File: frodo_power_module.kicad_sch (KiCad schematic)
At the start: 84 parts, among them J1 Keystone 1048, J10 SWD Header, J2 Molex MicroFit 2x3, J3 Molex MicroFit 2x2, J4 Molex MicroFit 2x2, J5 JST-GH, J6 JST-GH, J7 Molex MicroFit 2x3, U1 STM32F042F6Px, U2 L7805, U3 AZ1117I-3.3, U4 BQ25171-Q1, U5 BQ29200, U6 MCP2562-E-SN, U7 INA213, Y1 8MHz, 12p

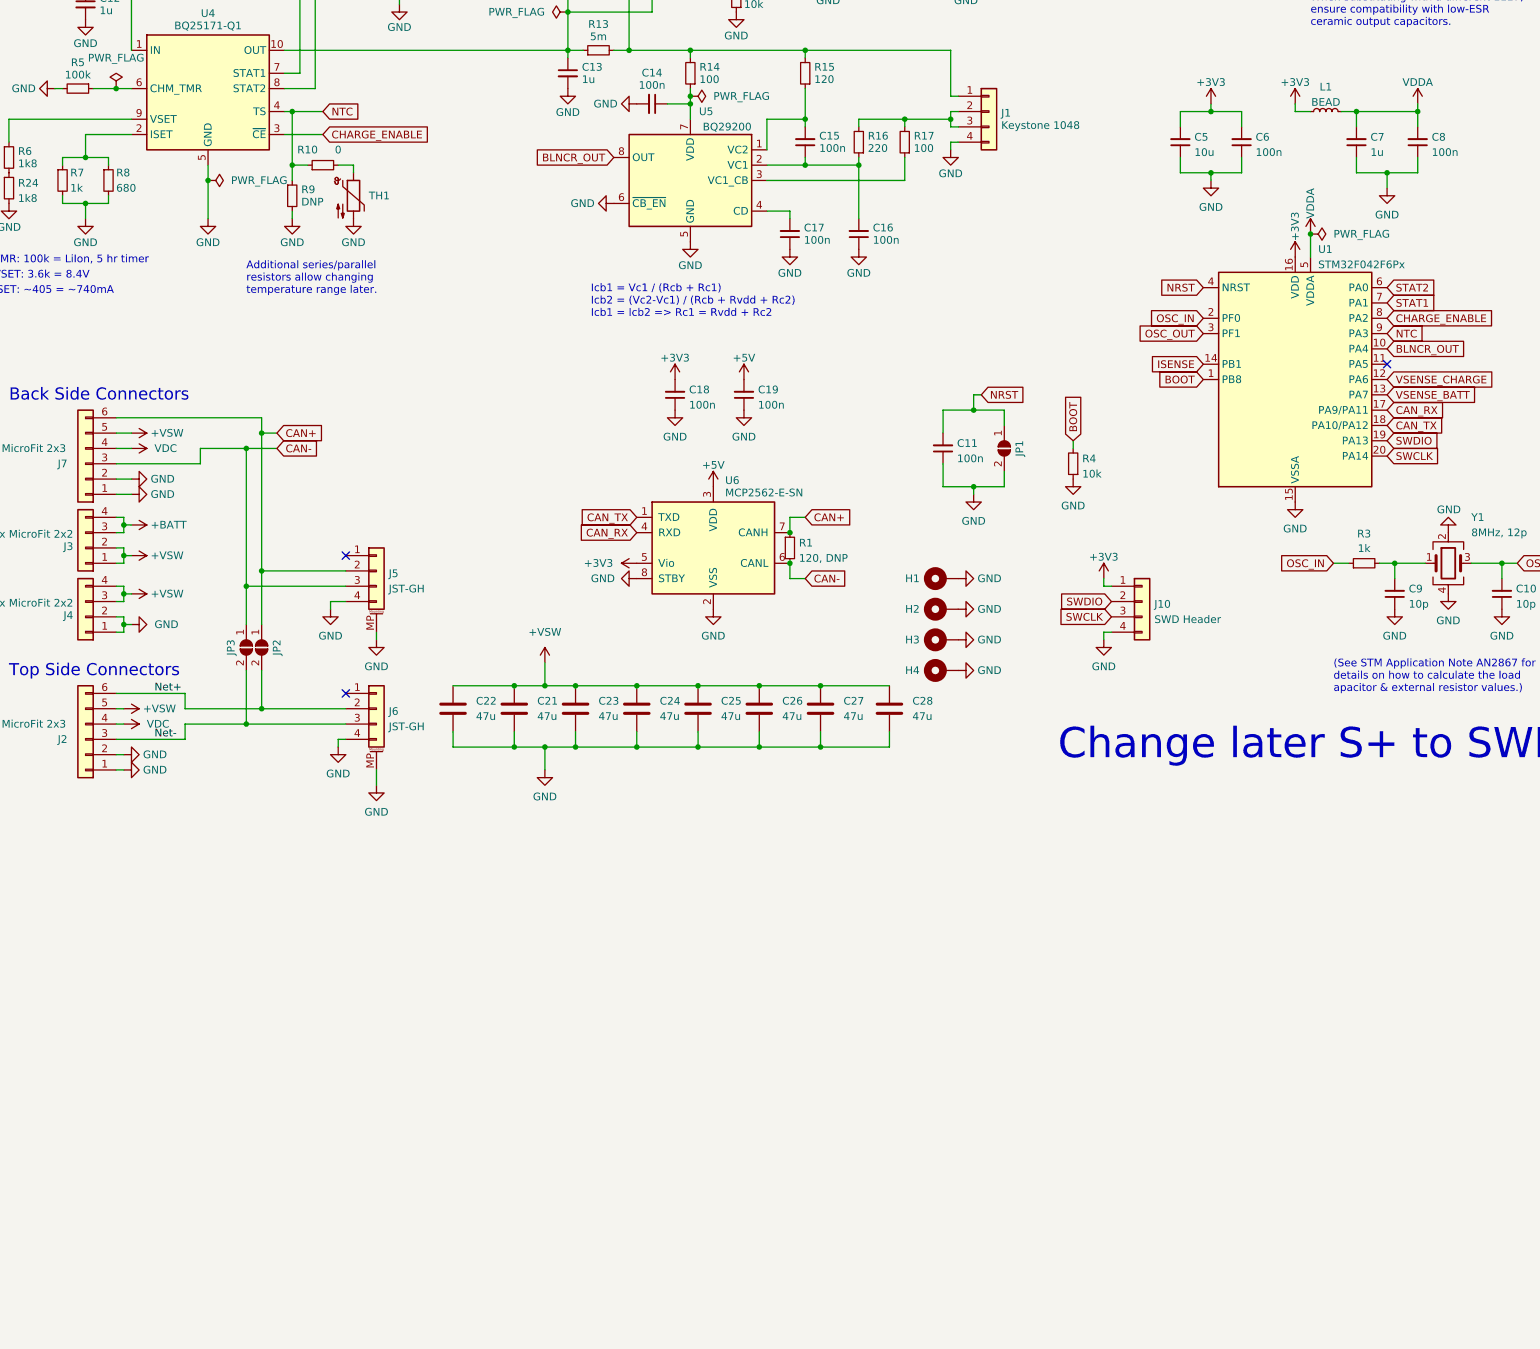
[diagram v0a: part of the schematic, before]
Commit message: Added 2 ICs to library, added these ICs to the schaltplan. Added Readme Notes
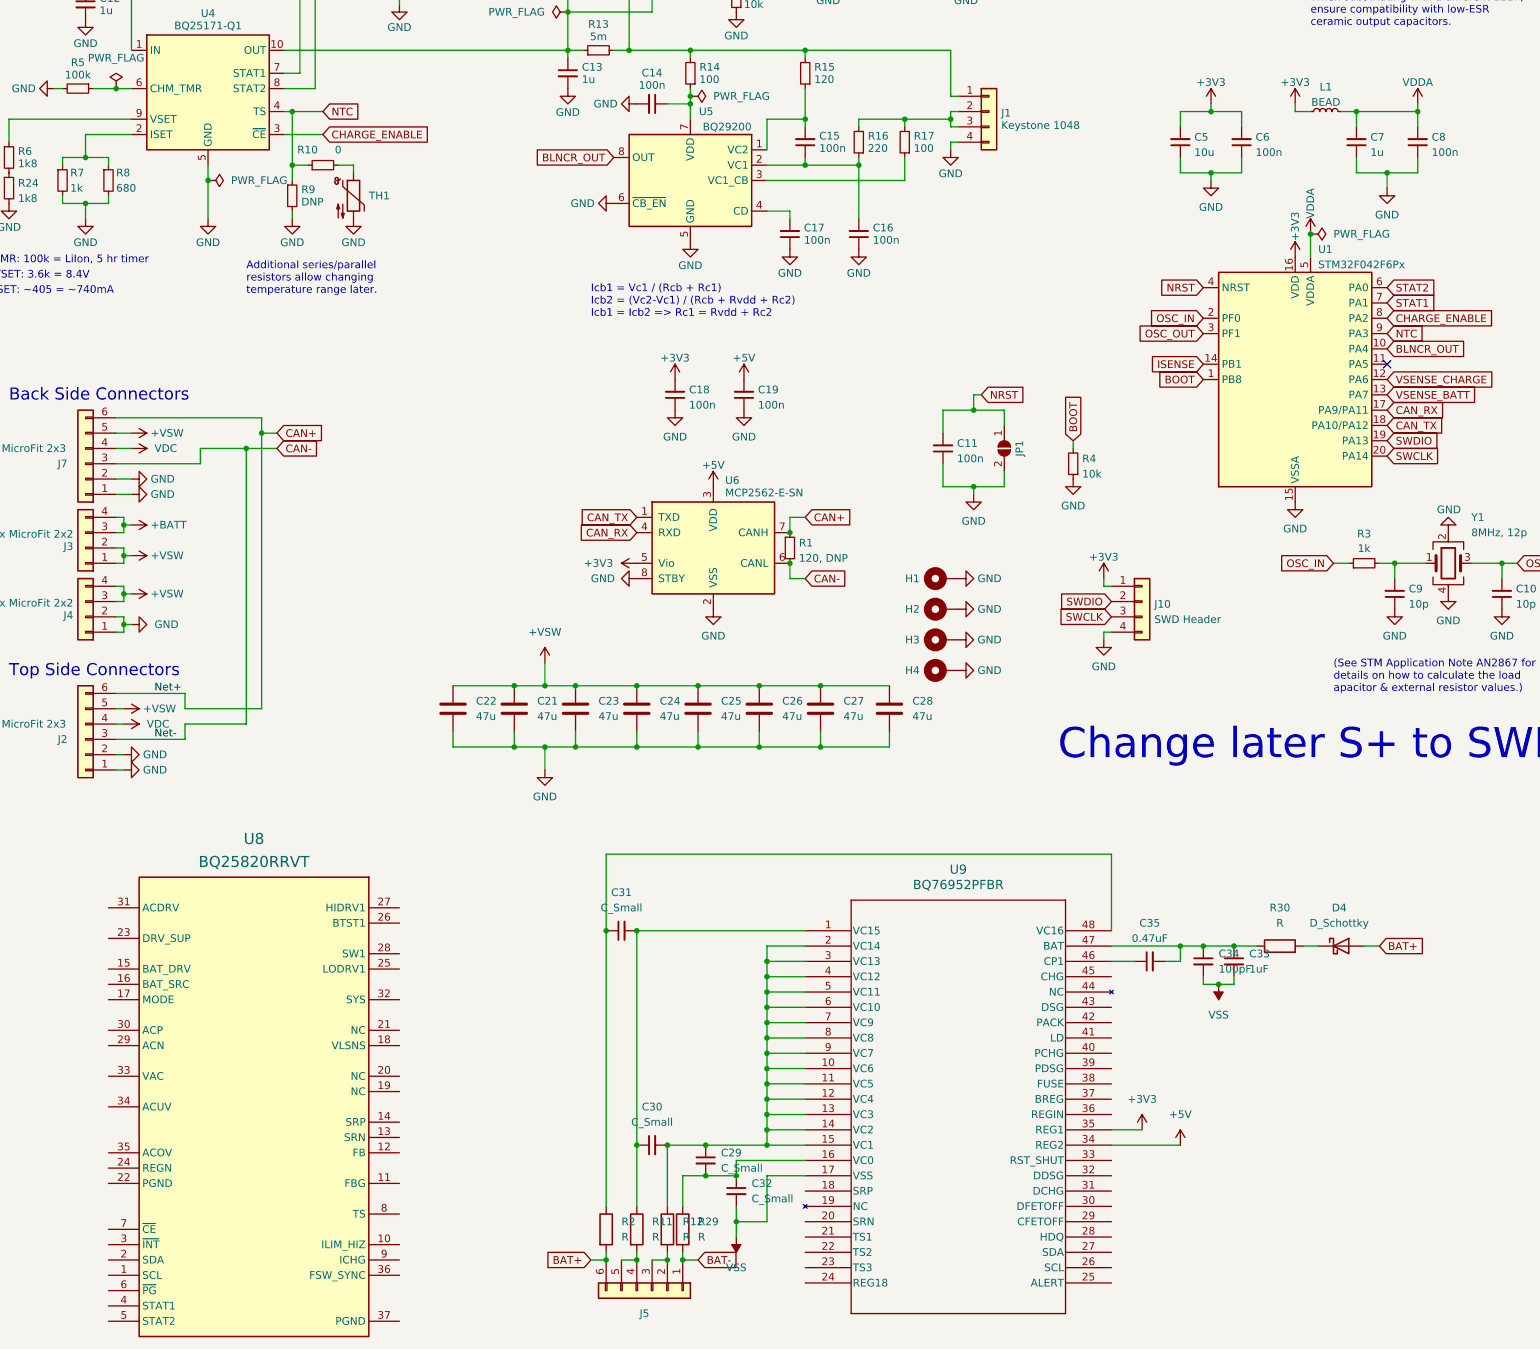
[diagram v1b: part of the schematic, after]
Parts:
- removed J5, J6: JST-GH, Connector_JST:JST_GH_SM04B-GHS-TB_1x04-1MP_P1.25mm_Horizontal, symbol Connector_Generic_MountingPin:Conn_01x04_MountingPin
- removed JP2, JP3: r, Jumper:SolderJumper-2_P1.3mm_Open_RoundedPad1.0x1.5mm, symbol Jumper:SolderJumper_2_Open
- added C29, C30, C31, C32: C_Small, symbol Device:C_Small
- added C33: 1uF, symbol Device:C_Small
- added C34: 100pF, symbol Device:C_Small
- added C35: 0.47uF, symbol Device:C_Small
- added D4: D_Schottky, symbol Device:D_Schottky
- added J5: Conn_01x06, symbol Connector_Generic:Conn_01x06
- added R11, R12, R2, R29, R30: R, symbol Device:R
- added U8: BQ25820RRVT, RRV0036A-IPC_B, symbol bq25820:CMP-0093461-2
- added U9: BQ76952PFBR, QFP_2PFBR_TEX, symbol bq76952:BQ76952PFBR
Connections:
- net Net+ is gone; now on net CAN+: J2.6 (Pin_6)
- net Net- is gone; now on net CAN-: J2.3 (Pin_3)
- net +3V3: now also U9.35 (REG1)
- net +5V: now also U9.34 (REG2)
- new net: C30.1, C31.2, R11.1, U9.1 (VC15)
- new net: J5.4 (Pin_4), J5.5 (Pin_5), R11.2
- new net: C33.1, C34.1, C35.2, R30.1, U9.47 (BAT)
- new net: D4.1 (K), R30.2
- new net: C31.1, R2.1, U9.48 (VC16)
- new net: J5.2 (Pin_2), J5.3 (Pin_3), R12.2
- new net: C29.1, C30.2, R12.1, U9.10 (VC6), U9.11 (VC5), U9.12 (VC4), U9.13 (VC3), U9.14 (VC2), U9.15 (VC1), U9.2 (VC14), U9.3 (VC13), U9.4 (VC12), U9.5 (VC11), U9.6 (VC10), U9.7 (VC9), U9.8 (VC8), U9.9 (VC7)
- new net: C29.2, C32.1, R29.1, U9.16 (VC0)
- new net: C35.1, U9.46 (CP1)
- new net BAT+: D4.2 (A), J5.6 (Pin_6), R2.2
- new net BAT-: J5.1 (Pin_1), R29.2
- new net VSS: C32.2, C33.2, C34.2, U9.17 (VSS)
- no-connect marks 3 -> 1

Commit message: Weitere Änderungen, aber noch nicht fertig
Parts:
- removed U8: BQ25820RRVT, RRV0036A-IPC_B, symbol bq25820:CMP-0093461-2
- added BUCK: ~, symbol Device:R_Small
- added C36, C50, C51: 0.1uF, symbol Device:C_Small
- added C37, C38, C44, C45: 100nF, symbol Device:C_Small
- added C39, C47, C48: 0.47uF, symbol Device:C_Small
- added C40: 2.2uF, symbol Device:C_Small
- added C41, C42: 80uF, symbol Device:C_Small
- added C43: 470nF, symbol Device:C_Small
- added C46, C49: 47nF, symbol Device:C_Small
- added D10, D11, D12, D7: D_Schottky, symbol Device:D_Schottky
- added D13: 16V, symbol Device:D_Schottky
- added D14: 100V, symbol Device:D
- added D8: LED, symbol Device:LED
- added D9: 10V, symbol Device:D_Schottky
- added F2: Fuse, symbol Device:Fuse
- added L2: L, symbol Device:L
- added Q1, Q10, Q11, Q12, Q2, Q3, Q4, Q5, Q6, Q7, Q8, Q9: NMOS, symbol Simulation_SPICE:NMOS
- added R31: 1M, symbol Device:R_Small
- added R32: 6.26k, symbol Device:R_Small
- added R33: 22.1k, symbol Device:R_Small
- added R34, R35, R37, R38: 10, symbol Device:R_Small
- added R36: 2, symbol Device:R_Small
- added R39, R46, R53: 7.5k, symbol Device:R_Small
- added R40: 12k, symbol Device:R_Small
- added R41: 250k, symbol Device:R_Small
- added R42: 30.31k, symbol Device:R_Small
- added R43: 3.3k, symbol Device:R_Small
- added R44: 4.2k, symbol Device:R_Small
- added R45: 80k, symbol Device:R_Small
- added R47: 20k, symbol Device:R_Small
- added R48, R50, R52, R54: 5.1k, symbol Device:R_Small
- added R49, R56: 10M, symbol Device:R_Small
- added R51, R55: R_Small, symbol Device:R_Small
- added R57: 10k, symbol Device:R_Small
- added R_AC_SNS: 2m, symbol Device:R_Small
- added R_BAT_SNS: 5m, symbol Device:R_Small
- added TP1, TP2, TP3, TP4: TestPoint, symbol Connector:TestPoint
- added U8: BQ25750RRVR, VQFN36_RRV_TEX, symbol bq25750:BQ25750RRVR
- C29, C30, C31, C32: value C_Small -> 220nF
- R11, R12, R2, R29: value R -> 20
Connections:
- net +5V: now also BUCK.1, C48.1, U8.23 (DRV_SUP)
- net +VSW: now also BUCK.2
- net BAT+: now also C50.1, D10.2 (A), D8.2 (A), Q10.3 (S), R37.2, R41.1, R49.1, R_BAT_SNS.2
- net BAT-: now also R42.2, U8.8 (TS)
- net VSS: now also C36.2, D9.2 (A), R33.2, R47.2
- new net: C51.2, D12.2 (A), D13.2 (A), Q11.3 (S), Q12.3 (S), R55.1, R56.1, TP3.1
- new net: C47.1, U8.24 (REGN)
- new net: D14.1 (K), Q12.1 (D), R51.2, R52.1, R53.1, R57.2, TP4.1
- new net: Q2.1 (D), R34.2, R_AC_SNS.1
- new net: D7.1 (K), Q1.2 (G), Q2.2 (G), U8.31 (ACDRV)
- new net: D7.2 (A), Q1.3 (S), Q2.3 (S)
- new net: C38.1, C39.1, R35.1, U8.29 (ACN)
- new net: C37.2, C39.2, R34.1, U8.30 (ACP)
- new net: R32.1, R33.1, U8.35 (ACOV)
- new net: R31.2, R32.2, U8.34 (ACUV)
- new net: D13.1 (K), Q12.2 (G), R56.2, R57.1
- new net: C43.1, C44.1, R37.1, U8.13 (SRN)
- new net: R52.2, R54.1
- new net: D11.1 (K), R54.2
- new net: Q9.1 (D), R46.2
- new net: C36.1, D9.1 (K), Q9.2 (G), R47.1, R48.2
- new net: D10.1 (K), Q10.2 (G), R49.2, R50.1, TP1.1
- new net: D8.1 (K), F2.1
- new net: F2.2, R39.1
- new net: R40.1, R41.2, U8.12 (FB)
- new net: R45.2, U8.36 (FSW_SYNC)
- new net: R38.2, R_BAT_SNS.1
- new net: C40.1, R36.1
- new net: R50.2, TP2.1
- new net: C42.1, Q4.1 (D), Q8.1 (D)
- new net: Q8.2 (G), U8.19 (HIDRV2)
- new net: C46.1, L2.2, Q7.1 (D), Q8.3 (S), U8.18 (SW2)
- new net: C49.1, L2.1, Q5.3 (S), Q6.1 (D), U8.28 (SW1)
- new net: C49.2, U8.26 (BTST1)
- new net: R43.2, U8.10 (ILIM_HIZ)
- new net: C43.2, C45.2, R38.1, U8.14 (SRP)
- new net: C41.2, Q3.1 (D), Q5.1 (D), R35.2, R36.2, R_AC_SNS.2, U8.32 (SYS)
- new net: Q5.2 (G), U8.27 (HIDRV1)
- new net: Q3.2 (G), Q4.2 (G), U8.15 (BATDRV)
- new net: Q3.3 (S), Q4.3 (S), U8.16 (BATSRC)
- new net: C46.2, U8.20 (BTST2)
- new net: D11.2 (A), R53.2
- new net: C50.2, C51.1
- new net: Q7.2 (G), U8.21 (LODRV2)
- new net: Q6.2 (G), U8.25 (LODRV1)
- new net: R39.2, R46.1
- new net: R44.2, U8.9 (ICHG)
- new net Earth: C37.1, C38.2, C40.2, C41.1, C42.2, C44.2, C45.1, C47.2, C48.2, Q6.3 (S), Q7.3 (S), R40.2, R42.1, R43.1, R44.1, R45.1, U8.17 (PGND), U8.22 (PGND)
- new net VAC: Q1.1 (D), R31.1, U8.33 (VAC)
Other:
- moved on the sheet: C1, C10, C11, C12, C13, C14, C15, C16, C17, C18, C19, C2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

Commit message: Zwischenstand
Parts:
- removed BUCK: ~, symbol Device:R_Small
- removed C29, C30, C31, C32: 220nF, symbol Device:C_Small
- removed C33: 1uF, symbol Device:C_Small
- removed C34: 100pF, symbol Device:C_Small
- removed C35, C39, C47, C48: 0.47uF, symbol Device:C_Small
- removed C36, C50, C51: 0.1uF, symbol Device:C_Small
- removed C37, C38, C44, C45: 100nF, symbol Device:C_Small
- removed C40: 2.2uF, symbol Device:C_Small
- removed C41, C42: 80uF, symbol Device:C_Small
- removed C43: 470nF, symbol Device:C_Small
- removed C46, C49: 47nF, symbol Device:C_Small
- removed D10, D11, D12, D4, D7: D_Schottky, symbol Device:D_Schottky
- removed D13: 16V, symbol Device:D_Schottky
- removed D14: 100V, symbol Device:D
- removed D8: LED, symbol Device:LED
- removed D9: 10V, symbol Device:D_Schottky
- removed F2: Fuse, symbol Device:Fuse
- removed J5: Conn_01x06, symbol Connector_Generic:Conn_01x06
- removed L2: L, symbol Device:L
- removed Q1, Q10, Q11, Q12, Q2, Q3, Q4, Q5, Q6, Q7, Q8, Q9: NMOS, symbol Simulation_SPICE:NMOS
- removed R11, R12, R2, R29: 20, symbol Device:R
- removed R30: R, symbol Device:R
- removed R31: 1M, symbol Device:R_Small
- removed R32: 6.26k, symbol Device:R_Small
- removed R33: 22.1k, symbol Device:R_Small
- removed R34, R35, R37, R38: 10, symbol Device:R_Small
- removed R36: 2, symbol Device:R_Small
- removed R39, R46, R53: 7.5k, symbol Device:R_Small
- removed R40: 12k, symbol Device:R_Small
- removed R41: 250k, symbol Device:R_Small
- removed R42: 30.31k, symbol Device:R_Small
- removed R43: 3.3k, symbol Device:R_Small
- removed R44: 4.2k, symbol Device:R_Small
- removed R45: 80k, symbol Device:R_Small
- removed R47: 20k, symbol Device:R_Small
- removed R48, R50, R52, R54: 5.1k, symbol Device:R_Small
- removed R49, R56: 10M, symbol Device:R_Small
- removed R51, R55: R_Small, symbol Device:R_Small
- removed R57: 10k, symbol Device:R_Small
- removed R_AC_SNS: 2m, symbol Device:R_Small
- removed R_BAT_SNS: 5m, symbol Device:R_Small
- removed TP1, TP2, TP3, TP4: TestPoint, symbol Connector:TestPoint
- removed U8: BQ25750RRVR, VQFN36_RRV_TEX, symbol bq25750:BQ25750RRVR
- removed U9: BQ76952PFBR, QFP_2PFBR_TEX, symbol bq76952:BQ76952PFBR
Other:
- added sheet New (V2.kicad_sch)
